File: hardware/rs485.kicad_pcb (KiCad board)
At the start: 2 copper layers, 40 x 40 mm, 50 parts, among them P1 CON-SENSOR2, P2 BOOT, P3 CONN_5, SW1 SW_DIP_4, U1 XMC1XXX48, U2 DRILL, U3 DRILL, U4 DRILL, U5 DRILL, U6 SP3491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

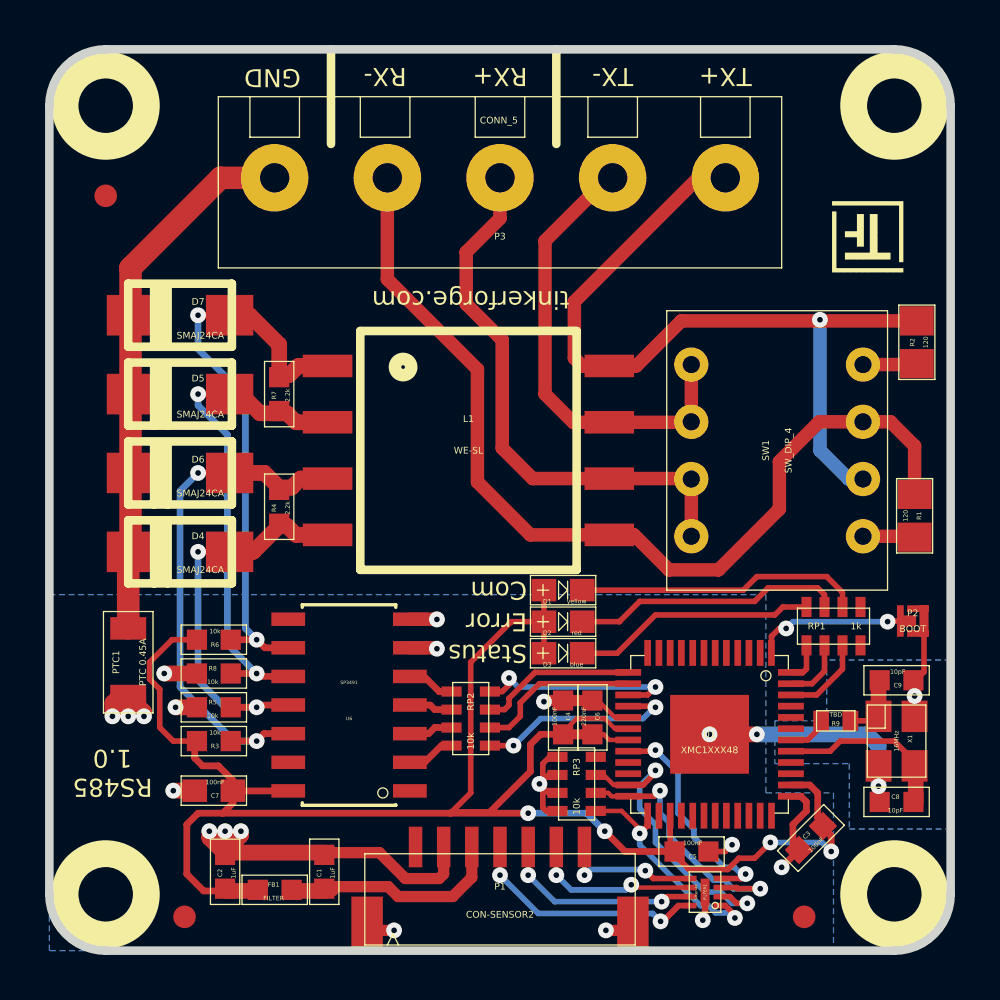
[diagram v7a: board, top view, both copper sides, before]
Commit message: change via diameter
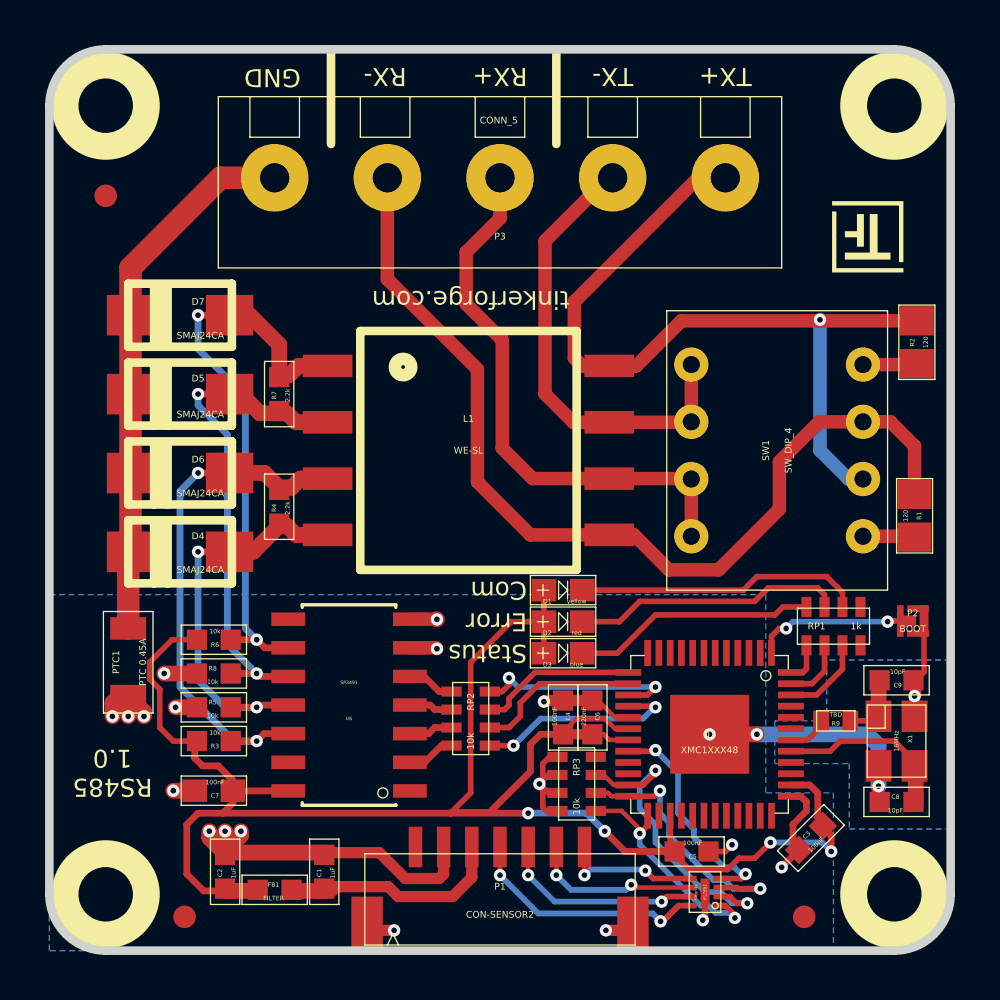
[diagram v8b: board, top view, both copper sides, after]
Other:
- net class Default: via_dia 0.70104 -> 0.55; via_drill 0.24892 -> 0.25
- rule via_min_drill: 0.24892 -> 0.25
- rule via_min_size: 0.70104 -> 0.5
